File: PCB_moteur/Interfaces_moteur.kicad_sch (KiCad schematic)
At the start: 20 parts, among them J2 Conn_01x06_Pin, J3 Conn_01x02, J5 Conn_01x04_Socket, J7 Conn_02x06_Top_Bottom, U2 ISOW1044, U4 LSF0204PWR, U9 INA333xxDGK

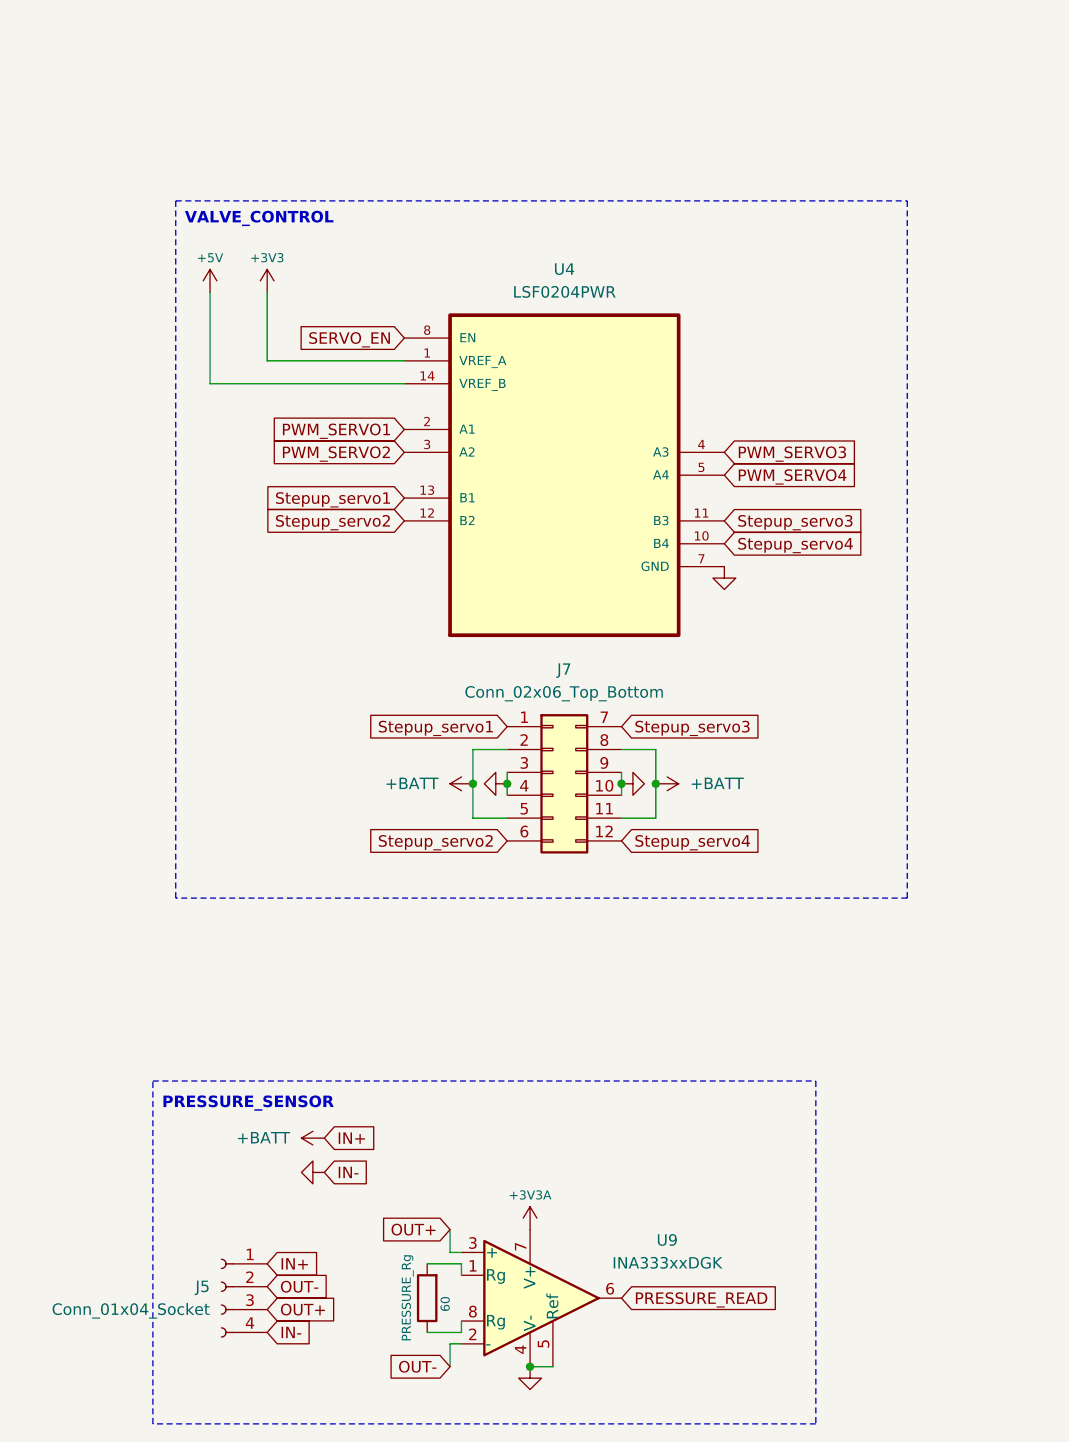
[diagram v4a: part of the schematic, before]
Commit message: fix: resistors + capacitances power supply
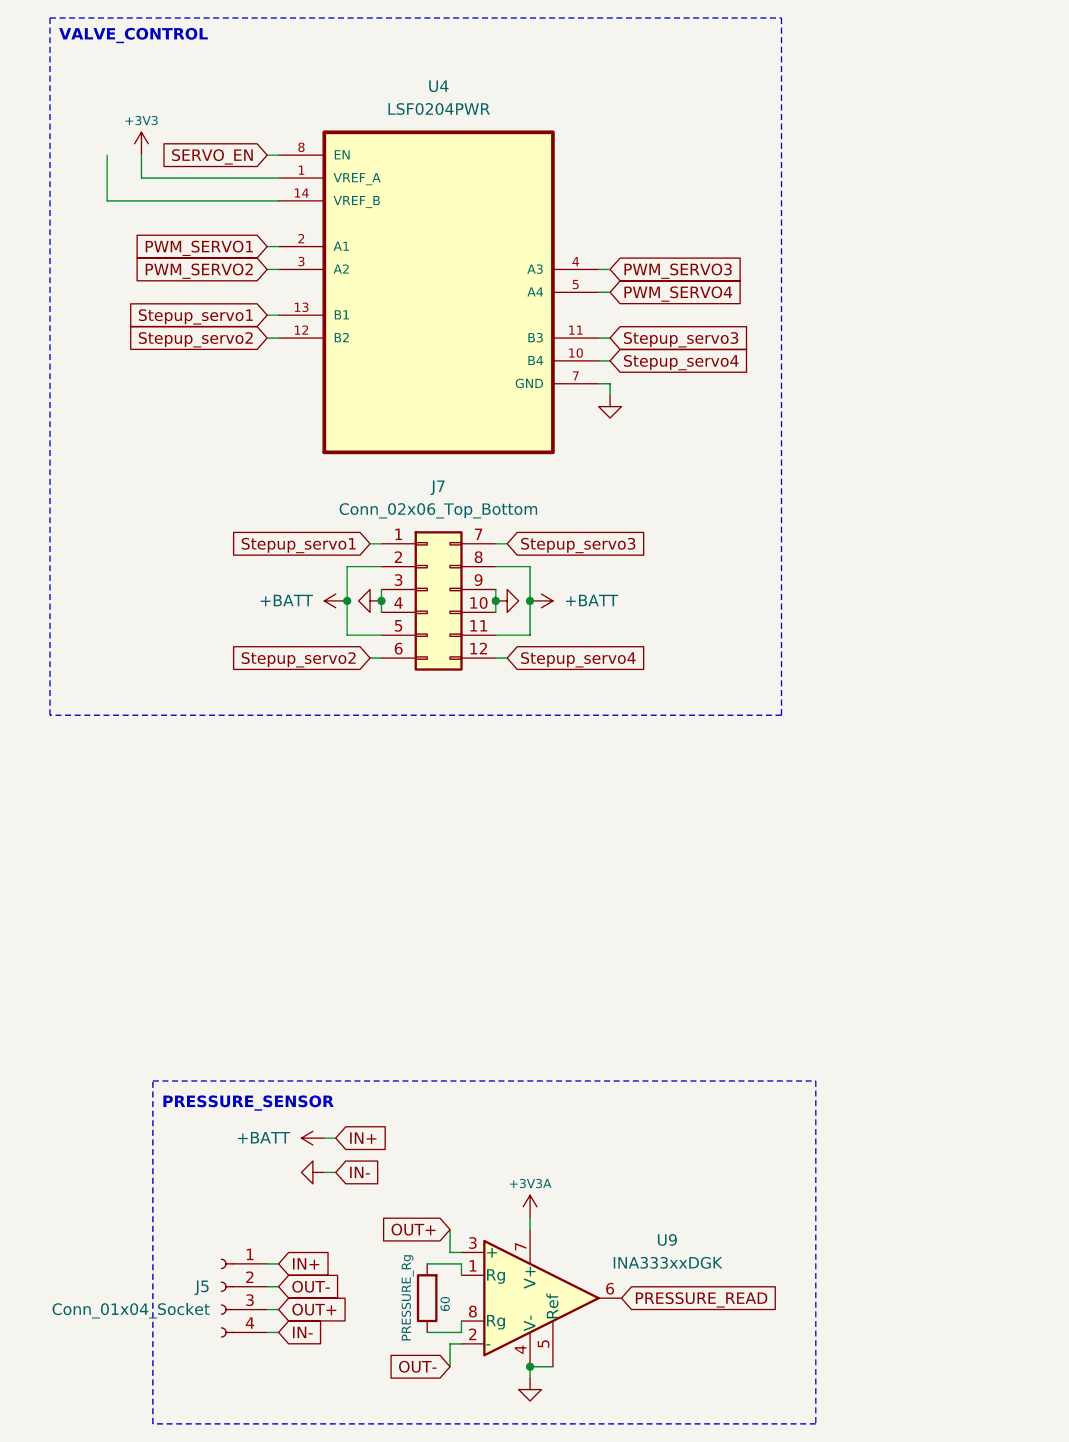
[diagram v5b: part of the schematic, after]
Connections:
- net +5V: no longer names the net of U4.14 (VREF_B)
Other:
- moved on the sheet: J7, U4

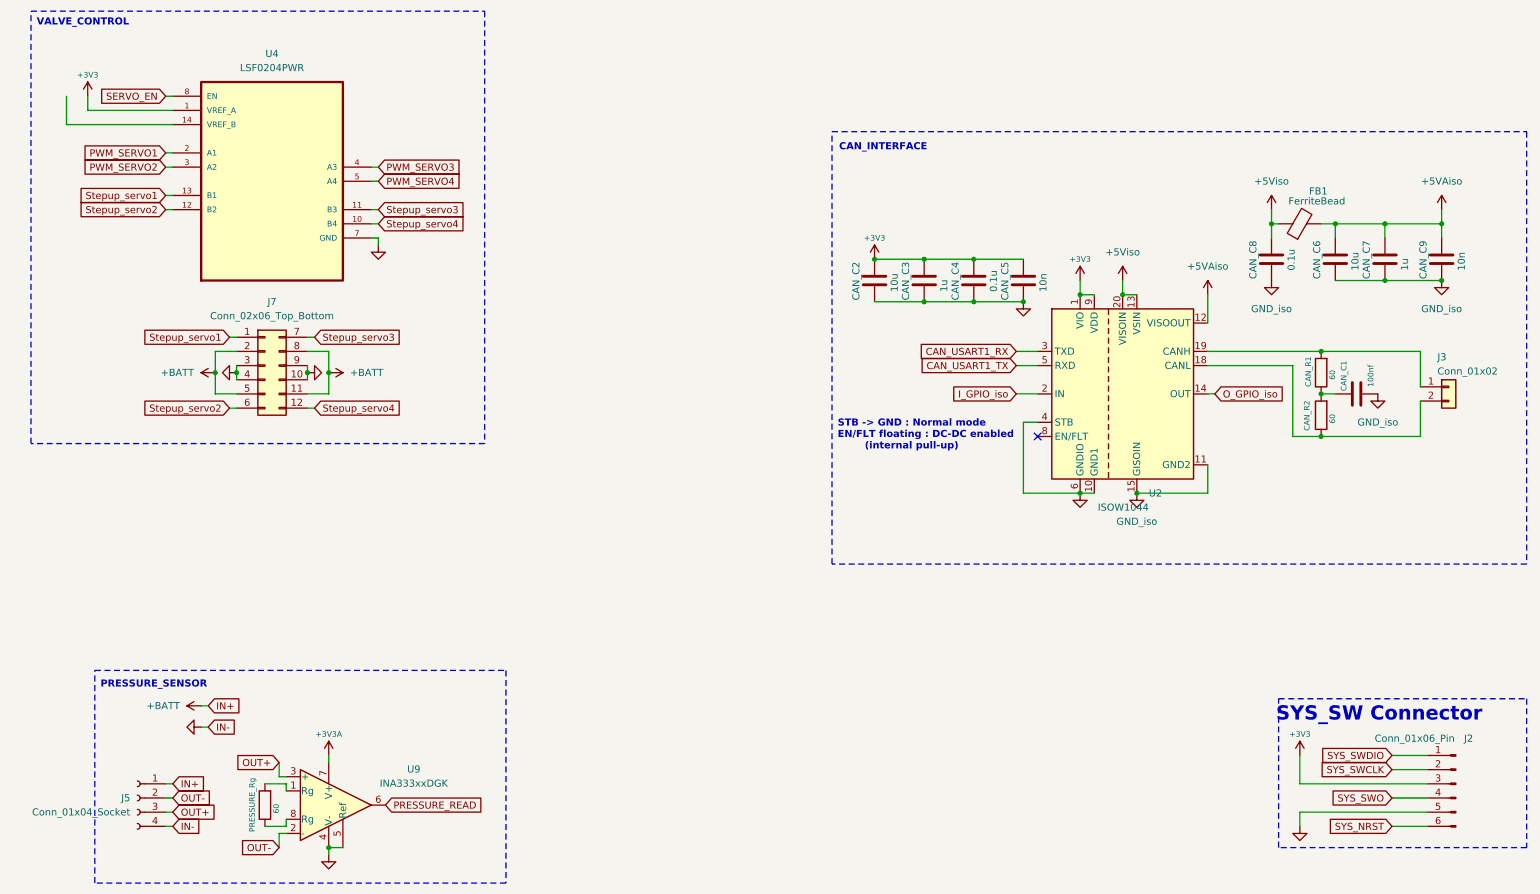
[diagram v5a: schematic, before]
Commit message: Added LDO, INA125, sensors
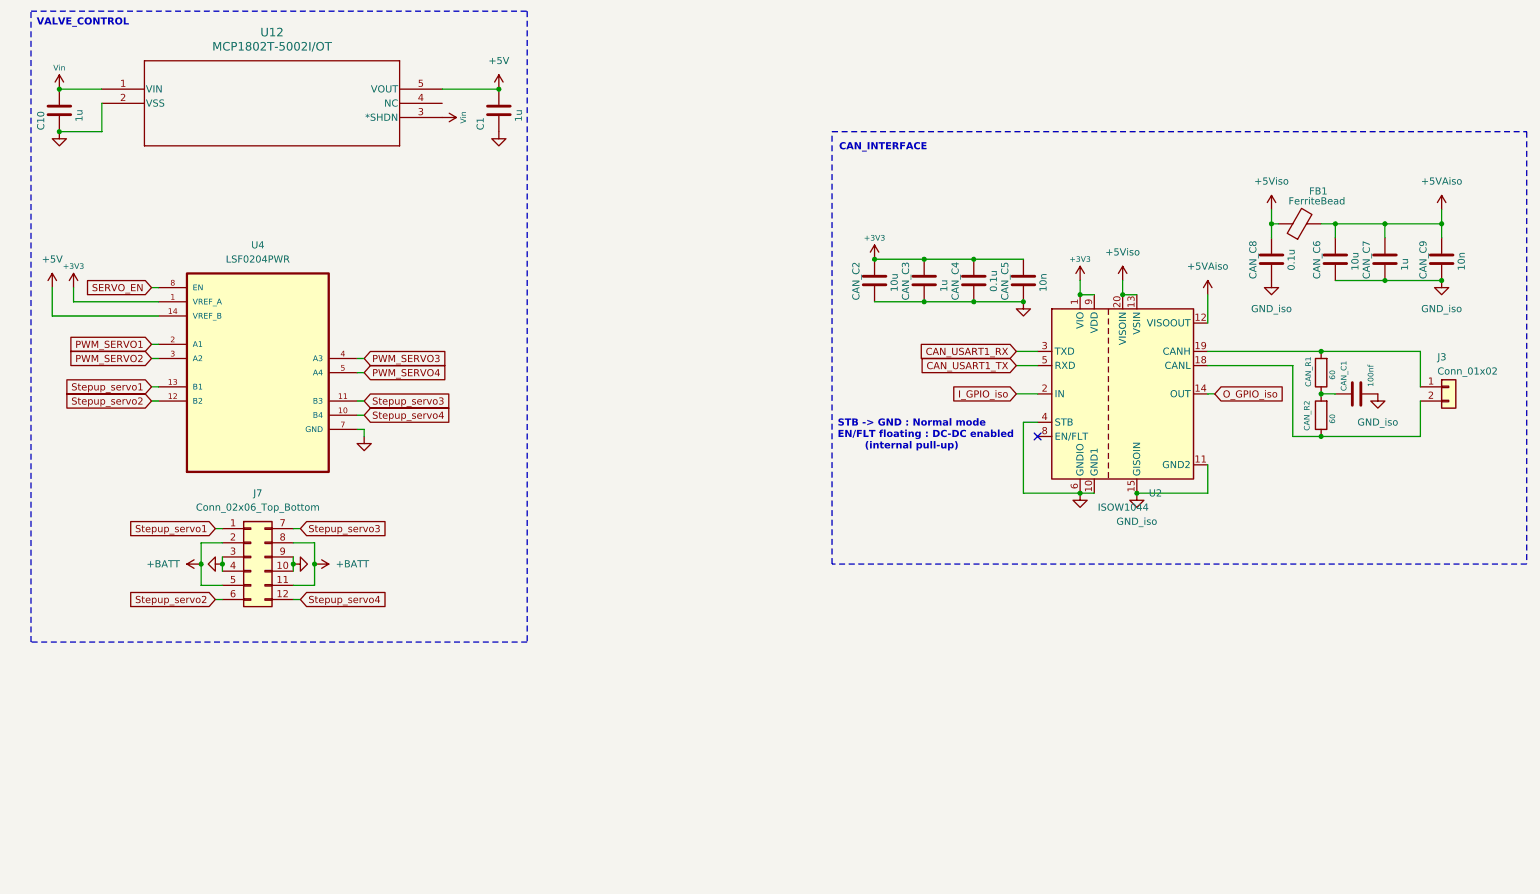
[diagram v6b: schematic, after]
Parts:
- removed J2: Conn_01x06_Pin, symbol Connector:Conn_01x06_Pin
- removed J5: Conn_01x04_Socket, symbol Connector:Conn_01x04_Socket
- removed PRESSURE_Rg: 60, Resistor_SMD:R_0805_2012Metric, symbol Device:R
- removed U9: INA333xxDGK, Package_SO:VSSOP-8_3x3mm_P0.65mm, symbol Amplifier_Instrumentation:INA333xxDGK
- added C1, C10: 1u, symbol Device:C
- added U12: MCP1802T-5002I/OT, SOT-23-5_MC_MCH, symbol 2026-01-14_15-06-07:MCP1802T-5002I_OT
- U4: DigiKey_Part_Number (none) -> 296-LSF0204PWRCT-ND; Manufacturer_Part_Number (none) -> LSF0204PWR
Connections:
- net GND: now also C1.2, C10.2, U12.2 (VSS)
- net +5V: now reaches U4.14 (VREF_B)
- net +5V: now also C1.1, U12.5 (VOUT)
- new net Vin: C10.1, U12.1 (VIN), U12.3 (*SHDN)
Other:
- note removed: "PRESSURE_SENSOR"
- note removed: "SYS_SW Connector"
- moved on the sheet: J7, U4

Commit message: modif mineure (pull-up, découplage)
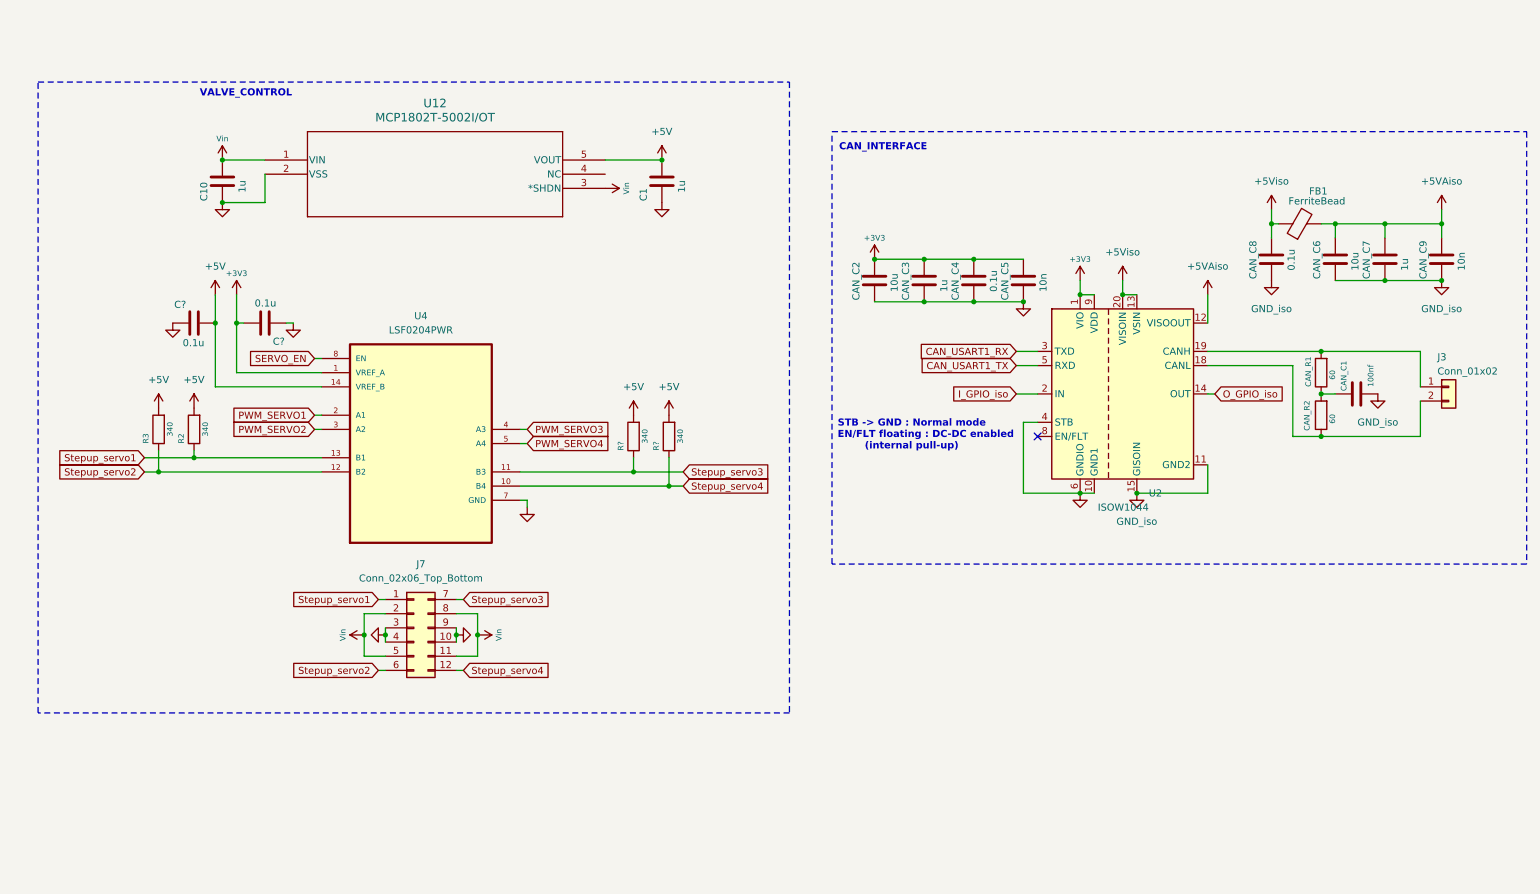
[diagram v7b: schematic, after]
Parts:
- added C? (x2): 0.1u, symbol Device:C
- added R2, R3, R? (x2): 340, Resistor_SMD:R_0805_2012Metric, symbol Device:R
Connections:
- net +BATT is gone; now on net Vin: J7.11 (Pin_11), J7.2 (Pin_2), J7.5 (Pin_5), J7.8 (Pin_8)
- net +3V3: now also C?.1
- net +5V: now also C?.1, R2.2, R3.2, R?.2, R?.2
- net GND: now also C?.2, C?.2
- net Stepup_servo1: now also R2.1
- net Stepup_servo2: now also R3.1
- net Stepup_servo3: now also R?.1
- net Stepup_servo4: now also R?.1
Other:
- moved on the sheet: C1, C10, J7, U12, U4

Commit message: fix: pyros resistors + typos +
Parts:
- gave numbers to parts that had none: 4
- renumbered C1 to C11
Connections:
- no-connect marks 1 -> 2
